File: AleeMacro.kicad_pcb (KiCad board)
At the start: 2 copper layers, 245.1 x 103.6 mm, 55 parts, among them U1 ProMicro

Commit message: Routing Adjustments
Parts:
- OLED: footprint Connector_PinHeader_2.54mm:PinHeader_1x04_P2.54mm_Vertical -> kbd:OLED_v2
- moved G*** 9.07 mm to (177.0, 61.0), turned to 90 degrees
- moved OLED 7.39 mm to (177.0, 83.8), turned to 0 degrees
- moved D10 6.19 mm to (167.4, 79.8), turned to 270 degrees
- moved D9 4.57 mm to (167.4, 97.5)
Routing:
- net Net-(D12-Pad2): track 5.91 -> 15.5 mm
- net VCC: track 26.4 -> 32.4 mm
- net COL3: track 58.8 -> 64.6 mm, vias 0 -> 1
- net Net-(SW1-Pad1): track 26.2 -> 31.5 mm
- net SDA: track 24.2 -> 29.4 mm
- net SCL: track 23.5 -> 25.8 mm
- net ROW2: track 65.3 -> 67.2 mm
- net ROW1: track 81.3 -> 80.1 mm
- net GND: track 76.3 -> 75.4 mm, vias 2 -> 0
- net Net-(D11-Pad2): track 7.37 -> 8.23 mm
- net COL0: track 141.5 -> 140.7 mm
- net ROW3: track 105.6 -> 106.2 mm
- net COL2: track 117.7 -> 117.3 mm, vias 0 -> 1
- net ROW0: vias 0 -> 2
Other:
- outline, holes or cut-outs redrawn
- board text removed: "He touched the butt."

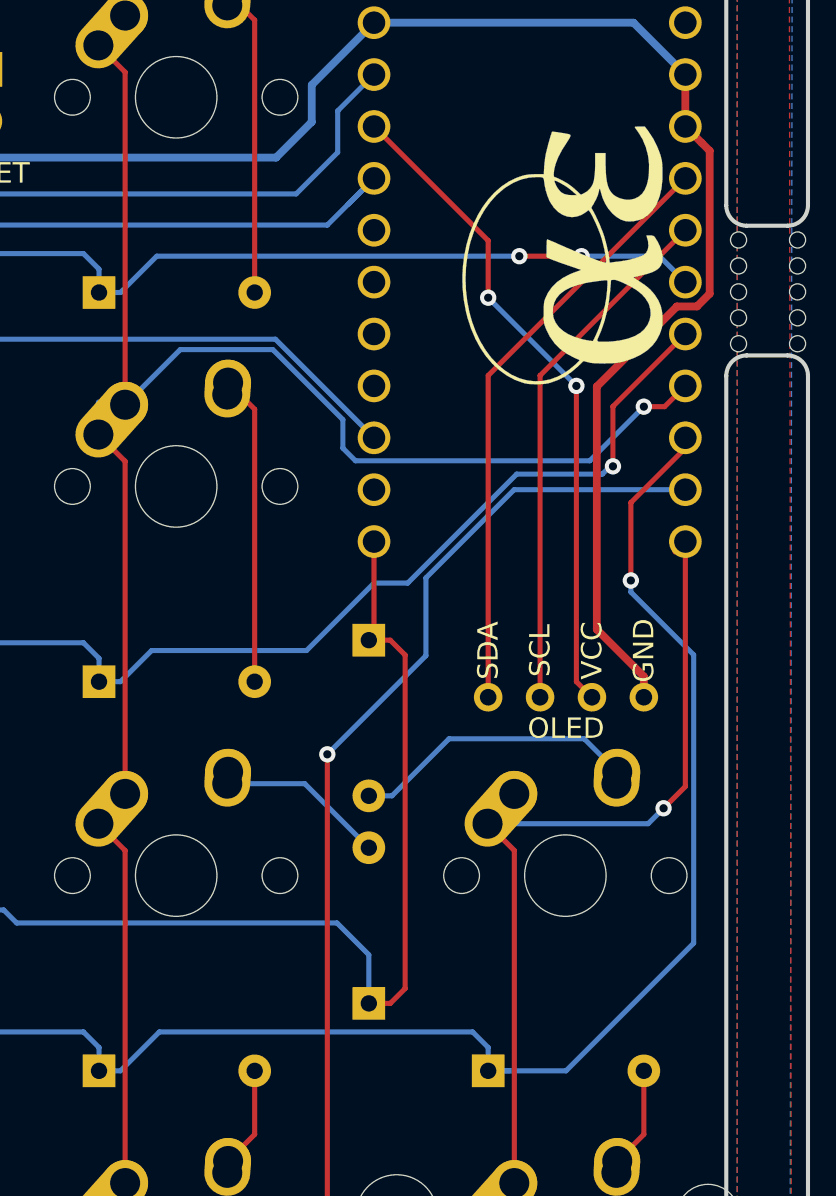
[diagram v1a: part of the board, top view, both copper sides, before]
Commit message: More routing and silks
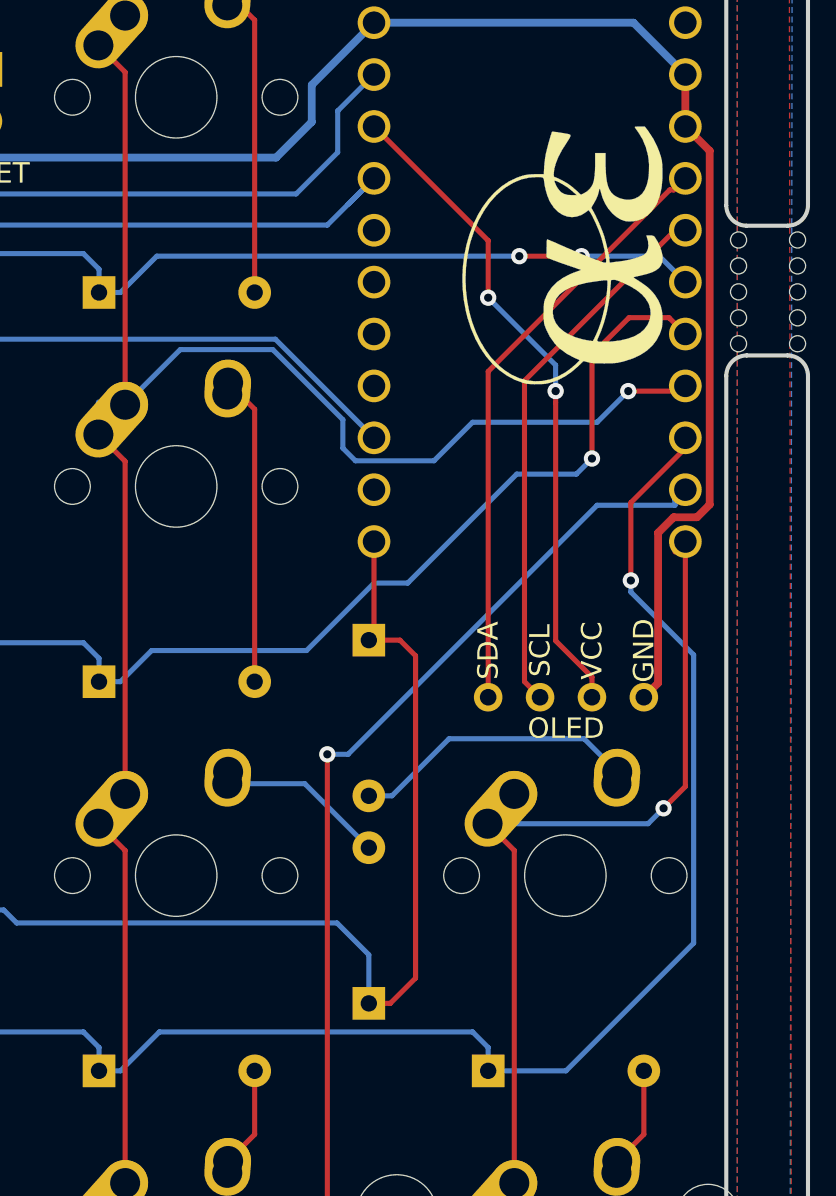
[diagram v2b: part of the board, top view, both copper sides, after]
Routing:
- net ROW1: track 80.1 -> 82.7 mm
- net ROW4: track 106.0 -> 103.9 mm
- net COL2: track 117.3 -> 119.2 mm
- net GND: track 75.4 -> 73.6 mm
- net ROW3: track 106.2 -> 105.2 mm
- net SCL: track 25.8 -> 26.7 mm
- net ROW2: track 67.2 -> 67.9 mm
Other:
- board text added: "He touched the butt."
